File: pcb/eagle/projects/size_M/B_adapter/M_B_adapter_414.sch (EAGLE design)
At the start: 8 parts

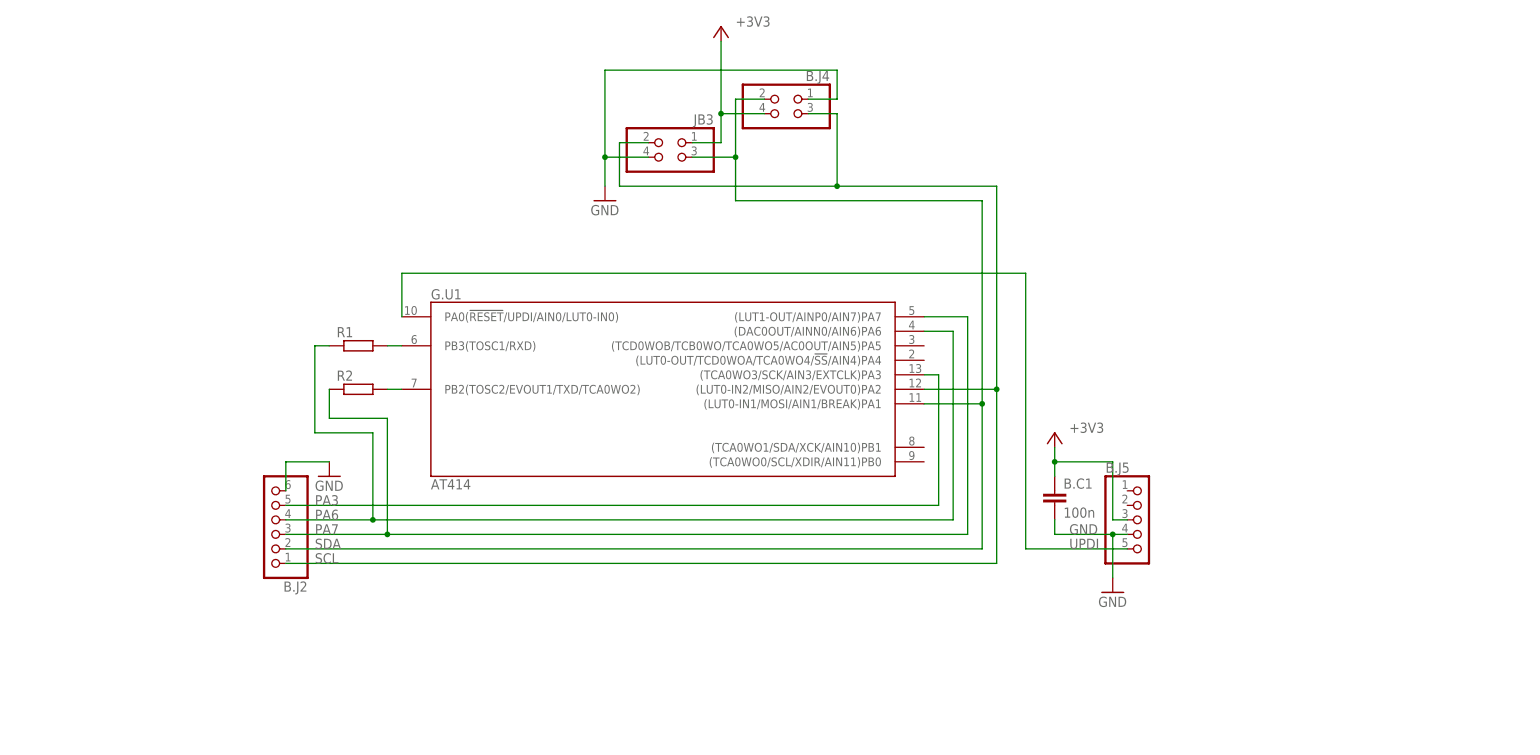
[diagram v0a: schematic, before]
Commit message: updated for PCB version 4
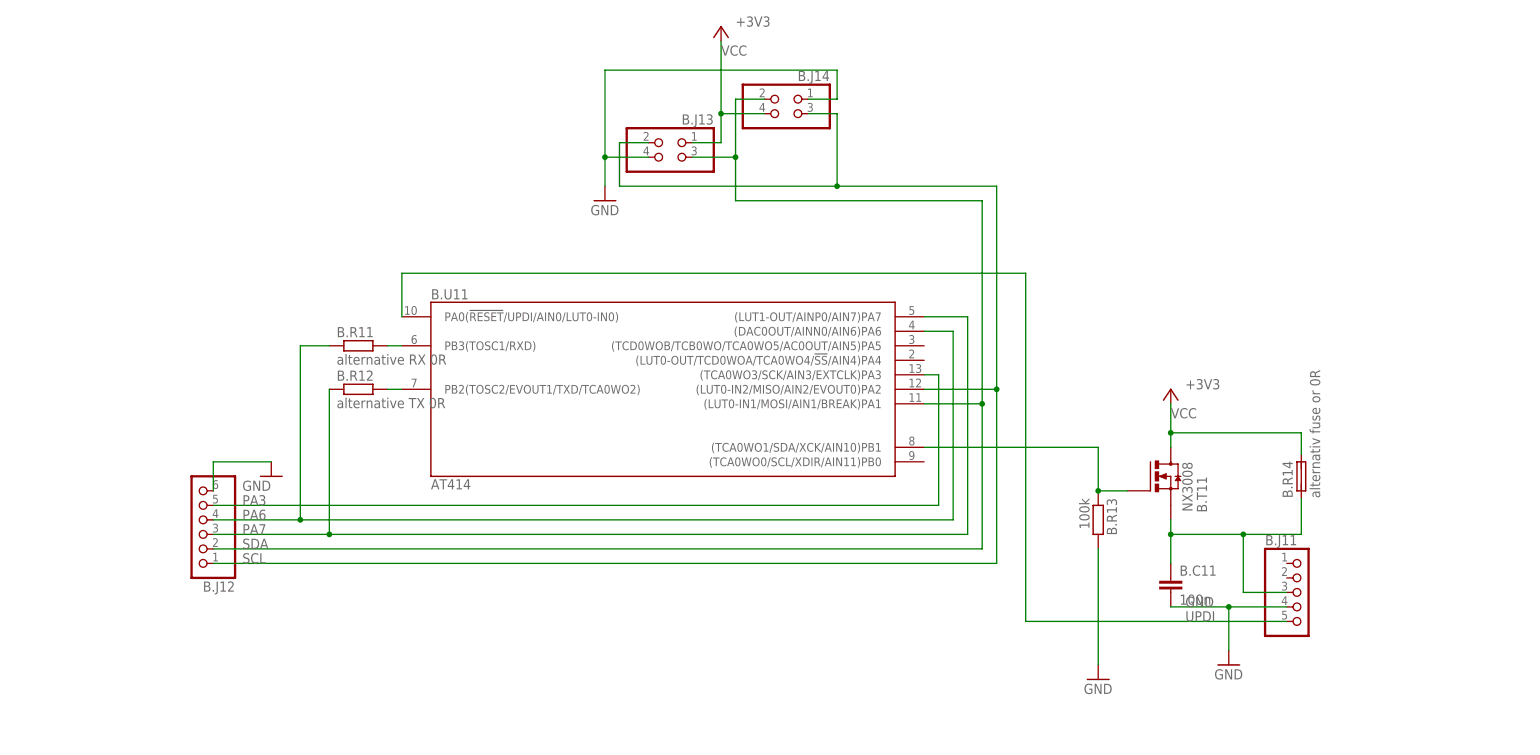
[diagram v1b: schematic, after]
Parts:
- removed B.C1: 100n, rcl:C-EUC0603
- removed B.J2: (no value), pinhead2:PINHD-1X6
- removed B.J5: (no value), pinhead2:PINHD-1X5
- added B.C11: 100n, rcl:C-EUC0603
- added B.J11: (no value), pinhead2:PINHD-1X5
- added B.J12: (no value), pinhead2:PINHD-1X6
- added B.R13: 100k, rcl:R-EU_R0603
- added B.R14: alternativ fuse or 0R, hugo:FUSE
- added B.T11: NX3008, hugo:N-MOSFET
- B.R11: value (none) -> alternative RX 0R
- B.R12: value (none) -> alternative TX 0R
- renumbered B.J4 to B.J14, G.U1 to B.U11, JB3 to B.J13, R1 to B.R11, R2 to B.R12
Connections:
- removed net 3V3: B.C1.1, B.J13.1, B.J14.4, B.J5.3
- new net N$3: B.R13.1, B.T11.G, B.U11G$1.(TCA0WO1/SDA/XCK/AIN10)PB1
- new net N$4: B.C11.1, B.J11.3, B.R14.1, B.T11.S
- new net VCC: B.J13.1, B.J14.4, B.R14.2, B.T11.D
- net GND: now also B.C11.2, B.J11.4, B.J12.6, B.R13.2; no longer B.C1.2, B.J2.6, B.J5.4
- net PA3: now also B.J12.5; no longer B.J2.5
- net PA6: now also B.J12.4; no longer B.J2.4
- net PA7: now also B.J12.3; no longer B.J2.3
- net SCL: now also B.J12.1; no longer B.J2.1
- net SDA: now also B.J12.2; no longer B.J2.2
- net UPDI: now also B.J11.5; no longer B.J5.5
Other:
- note removed: "RX + TX"

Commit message: collection of PCBs for v4 started
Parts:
- B.R11: value alternative RX 0R -> alt RX 0R
- B.R12: value alternative TX 0R -> alt TX 0R
- B.R14: value alternativ fuse or 0R -> alt fuse or 0R
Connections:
- new net VBAT: B.J11.2
- new net VUSB: B.J11.1
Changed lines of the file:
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@@
 <part name="GND3" library="supply1" library_urn="urn:adsk.eagle:library:371" deviceset="GND" device=""/>
 <part name="B.U11" library="atmel" deviceset="ATTINY*14" device="-SSN" technology="4" value="AT414"/>
-<part name="B.R11" library="rcl" library_urn="urn:adsk.eagle:library:334" deviceset="R-EU_" device="R0603" package3d_urn="urn:adsk.eagle:package:23555/3" value="alternative RX 0R"/>
-<part name="B.R12" library="rcl" library_urn="urn:adsk.eagle:library:334" deviceset="R-EU_" device="R0603" package3d_urn="urn:adsk.eagle:package:23555/3" value="alternative TX 0R"/>
+<part name="B.R11" library="rcl" library_urn="urn:adsk.eagle:library:334" deviceset="R-EU_" device="R0603" package3d_urn="urn:adsk.eagle:package:23555/3" value="alt RX 0R"/>
+<part name="B.R12" library="rcl" library_urn="urn:adsk.eagle:library:334" deviceset="R-EU_" device="R0603" package3d_urn="urn:adsk.eagle:package:23555/3" value="alt TX 0R"/>
 <part name="B.T11" library="hugo" deviceset="N-MOSFET" device="" value="NX3008"/>
 <part name="B.R13" library="rcl" library_urn="urn:adsk.eagle:library:334" deviceset="R-EU_" device="R0603" package3d_urn="urn:adsk.eagle:package:23555/3" value="100k"/>
 <part name="GND4" library="supply1" library_urn="urn:adsk.eagle:library:371" deviceset="GND" device=""/>
 <part name="+3V1" library="supply1" library_urn="urn:adsk.eagle:library:371" deviceset="+3V3" device=""/>
-<part name="B.R14" library="hugo" deviceset="FUSE" device="" value="alternativ fuse or 0R"/>
+<part name="B.R14" library="hugo" deviceset="FUSE" device="" value="alt fuse or 0R"/>
 </parts>
 <sheets>
@@
 </segment>
 </net>
+<net name="VUSB" class="0">
+<segment>
+<pinref part="B.J11" gate="A" pin="1"/>
+<wire x1="223.52" y1="-2.54" x2="218.44" y2="-2.54" width="0.1524" layer="91"/>
+</segment>
+</net>
+<net name="VBAT" class="0">
+<segment>
+<pinref part="B.J11" gate="A" pin="2"/>
+<wire x1="223.52" y1="-5.08" x2="218.44" y2="-5.08" width="0.1524" layer="91"/>
+</segment>
+</net>

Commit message: minor fixes
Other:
- note added: "* R11(R12) are used when TX(RX) are asked. * PA6 and PA7 are in the high impedance state in this case."
- note added: "* br14 is used if the transistor is not used. * it can be replaced by a fuse as well * b15 is not used when the trasistor is not used"
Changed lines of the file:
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@@
 <sheet>
 <plain>
+<text x="193.04" y="33.02" size="1.778" layer="97">* br14 is used if the transistor is not used.
+* it can be replaced by a fuse as well
+* b15 is not used when the trasistor is not used</text>
+<text x="101.6" y="55.88" size="1.778" layer="97" rot="R180">* R11(R12) are used when TX(RX) are asked.
+* PA6 and PA7 are in the high impedance state in this case. </text>
 </plain>
 <instances>
@@
 </drawing>
 <compatibility>
+<note version="6.3" minversion="6.2.2" severity="warning">
+Since Version 6.2.2 text objects can contain more than one line,
+which will not be processed correctly with this version.
+</note>
 <note version="8.2" severity="warning">
 Since Version 8.2, EAGLE supports online libraries. The ids

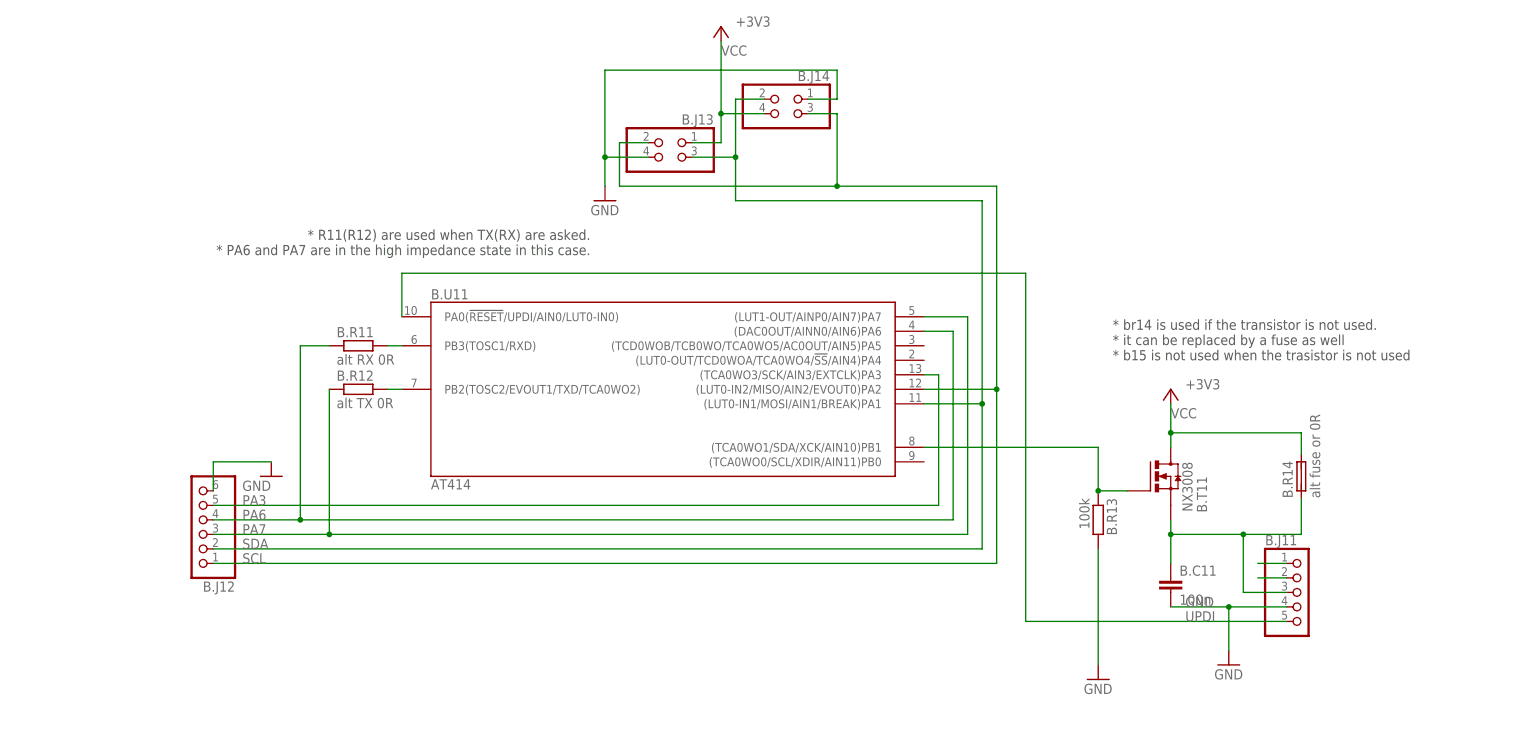
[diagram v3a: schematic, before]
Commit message: bugfix: switched serial TX-RX
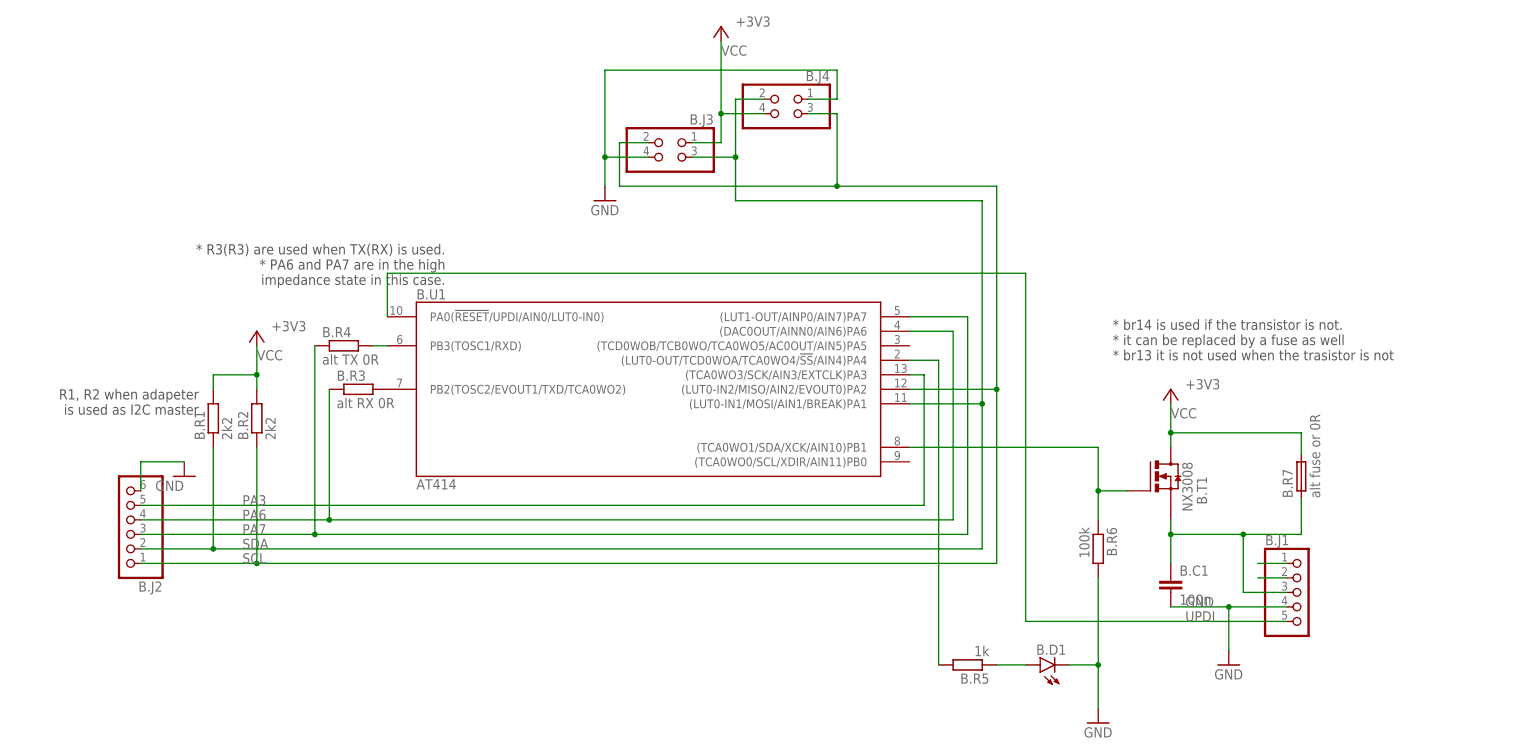
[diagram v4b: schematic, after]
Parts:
- removed B.J12: (no value), pinhead2:PINHD-1X6
- removed B.R11: alt RX 0R, rcl:R-EU_R0603
- removed B.R13: 100k, rcl:R-EU_R0603
- removed B.U11: AT414, atmel:ATTINY414-SSN
- added B.D1: (no value), led:LEDCHIP-LED0603
- added B.J2: (no value), pinhead2:PINHD-1X6
- added B.R1, B.R2: 2k2, rcl:R-EU_R0603
- added B.R4: alt TX 0R, rcl:R-EU_R0603
- added B.R5: 1k, rcl:R-EU_R0603
- added B.R6: 100k, rcl:R-EU_R0603
- added B.U1: AT414, atmel:ATTINY414-SSN
- B.R3: value alt TX 0R -> alt RX 0R
- renumbered B.C11 to B.C1, B.J11 to B.J1, B.J13 to B.J3, B.J14 to B.J4, B.R12 to B.R3, B.R14 to B.R7, B.T11 to B.T1
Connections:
- new net N$5: B.R5.2, B.U1G$1.(LUT0-OUT/TCD0WOA/TCA0WO4/!SS!/AIN4)PA4
- new net PA1: B.D1.A, B.R5.1
- net GND: now also B.D1.C, B.J2.6, B.R6.2; no longer B.J12.6, B.R13.2
- net N$1: now also B.R4.2, B.U1G$1.PB3(TOSC1/RXD); no longer B.R3.2, B.U11G$1.PB2(TOSC2/EVOUT1/TXD/TCA0WO2)
- net N$2: now also B.R3.2, B.U1G$1.PB2(TOSC2/EVOUT1/TXD/TCA0WO2); no longer B.R11.2, B.U11G$1.PB3(TOSC1/RXD)
- net N$3: now also B.R6.1, B.U1G$1.(TCA0WO1/SDA/XCK/AIN10)PB1; no longer B.R13.1, B.U11G$1.(TCA0WO1/SDA/XCK/AIN10)PB1
- net PA3: now also B.J2.5, B.U1G$1.(TCA0WO3/SCK/AIN3/EXTCLK)PA3; no longer B.J12.5, B.U11G$1.(TCA0WO3/SCK/AIN3/EXTCLK)PA3
- net PA6: now also B.J2.4, B.R3.1, B.U1G$1.(DAC0OUT/AINN0/AIN6)PA6; no longer B.J12.4, B.R11.1, B.U11G$1.(DAC0OUT/AINN0/AIN6)PA6
- net PA7: now also B.J2.3, B.R4.1, B.U1G$1.(LUT1-OUT/AINP0/AIN7)PA7; no longer B.J12.3, B.R3.1, B.U11G$1.(LUT1-OUT/AINP0/AIN7)PA7
- net SCL: now also B.J2.1, B.R2.1, B.U1G$1.(LUT0-IN2/MISO/AIN2/EVOUT0)PA2; no longer B.J12.1, B.U11G$1.(LUT0-IN2/MISO/AIN2/EVOUT0)PA2
- net SDA: now also B.J2.2, B.R1.1, B.U1G$1.(LUT0-IN1/MOSI/AIN1/BREAK)PA1; no longer B.J12.2, B.U11G$1.(LUT0-IN1/MOSI/AIN1/BREAK)PA1
- net UPDI: now also B.U1G$1.PA0(!RESET!/UPDI/AIN0/LUT0-IN0); no longer B.U11G$1.PA0(!RESET!/UPDI/AIN0/LUT0-IN0)
- net VCC: now also B.R1.2, B.R2.2
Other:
- note added: "* R3(R3) are used when TX(RX) is used. * PA6 and PA7 are in the high impedance state in this case."
- note added: "* br14 is used if the transistor is not. * it can be replaced by a fuse as well * br13 it is not used when the trasistor is not"
- note added: "R1, R2 when adapeter is used as I2C master"
- note removed: "* R11(R12) are used when TX(RX) are asked. * PA6 and PA7 are in the high impedance state in this case."
- note removed: "* br14 is used if the transistor is not used. * it can be replaced by a fuse as well * b15 is not used when the trasistor is not used"

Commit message: minor changes for PCB v6.
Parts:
- added B.C12: 100n, rcl:C-EUC0603
- renumbered B.C1 to B.C11, B.D1 to B.D11, B.R1 to B.R11, B.R2 to B.R12, B.R3 to B.R13, B.R4 to B.R14, B.R5 to B.R15, B.R6 to B.R16, B.R7 to B.R17, B.T1 to B.T11, B.U1 to B.U11
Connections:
- net GND: now also B.C12.2
- net VCC: now also B.C12.1
